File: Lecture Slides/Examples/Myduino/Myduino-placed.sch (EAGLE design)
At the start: 30 parts, among them J2 GENERIC-BATTERY-CONN-RECEPTAC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, Y1 16MHz

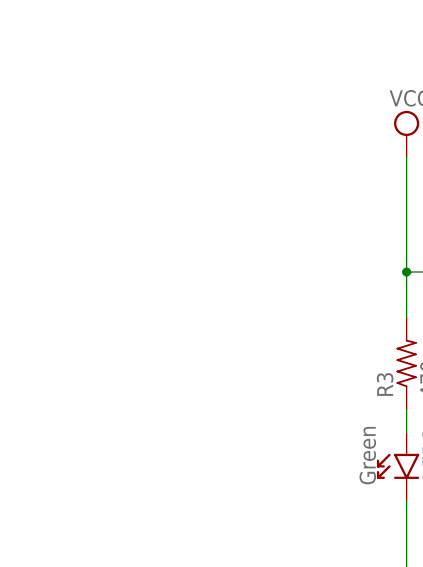
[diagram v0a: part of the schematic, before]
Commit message: gitignore.  update examples
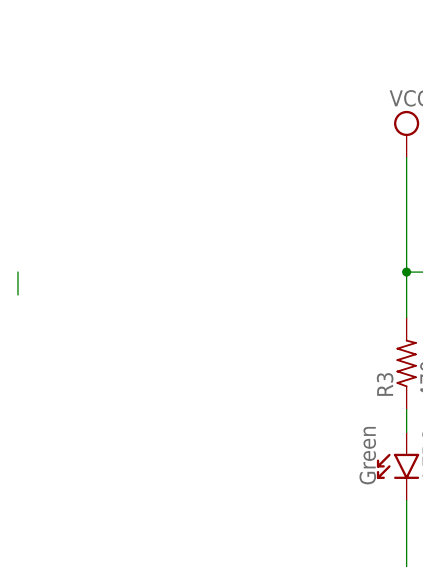
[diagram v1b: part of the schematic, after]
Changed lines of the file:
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@@
 <?xml version="1.0" encoding="utf-8"?>
 <!DOCTYPE eagle SYSTEM "eagle.dtd">
-<eagle version="7.2.0">
+<eagle version="7.6.0">
 <drawing>
 <settings>
@@
 <layer number="56" name="wert" color="7" fill="1" visible="no" active="no"/>
 <layer number="57" name="tCAD" color="7" fill="1" visible="no" active="no"/>
+<layer number="59" name="tFaceplate" color="11" fill="1" visible="no" active="no"/>
+<layer number="60" name="bFaceplate" color="13" fill="1" visible="no" active="no"/>
 <layer number="90" name="Modules" color="5" fill="1" visible="yes" active="yes"/>
 <layer number="91" name="Nets" color="2" fill="1" visible="yes" active="yes"/>
@@
 <layer number="98" name="Guide" color="6" fill="1" visible="yes" active="yes"/>
 <layer number="9" name="Route9" color="4" fill="2" visible="no" active="no"/>
+<layer number="169" name="internal" color="7" fill="1" visible="yes" active="yes"/>
 <layer number="199" name="Contour" color="7" fill="1" visible="yes" active="yes"/>
 <layer number="200" name="200bmp" color="1" fill="10" visible="yes" active="yes"/>
@@
 <instance part="D5" gate="G$1" x="99.06" y="30.48" rot="R270"/>
 <instance part="D6" gate="G$1" x="71.12" y="30.48" rot="R270"/>
-<instance part="FRAME9" gate="G$1" x="-2.54" y="0"/>
+<instance part="FRAME9" gate="G$1" x="-20.32" y="-27.94"/>
 <instance part="FTDI" gate="G$1" x="132.08" y="165.1" rot="R180"/>
 <instance part="GND1" gate="1" x="71.12" y="-2.54" rot="MR0"/>
@@
 </segment>
 </net>
+<net name="N$1" class="0">
+<segment>
+<wire x1="2.54" y1="127" x2="2.54" y2="124.46" width="0.1524" layer="91"/>
+</segment>
+</net>
